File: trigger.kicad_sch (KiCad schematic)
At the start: 0 parts

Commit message: Chose amplifiers
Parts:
- added R23: R, symbol Device:R
- added U2: LTC6754xSC6, Package_TO_SOT_SMD:SOT-363_SC-70-6, symbol Comparator:LTC6754xSC6
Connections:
- new net: R23.1, U2.3 (+)
- new net AN_TRIGGER: U2.4 (-)
- new net AN_TRIGGER_N: U2.6 (~{Q})
- new net AN_TRIGGER_P: U2.1 (Q)
- new net TRIGGER_LEVEL: R23.2

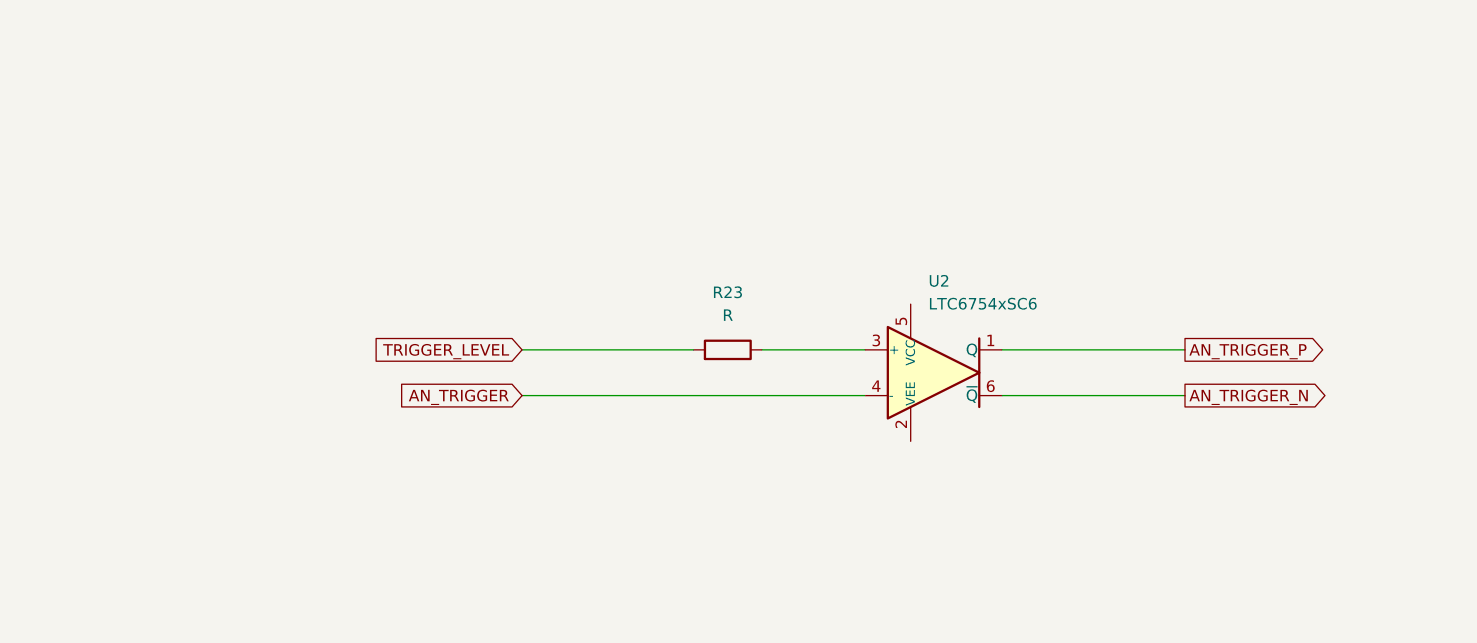
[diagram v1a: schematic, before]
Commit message: Move the trigger
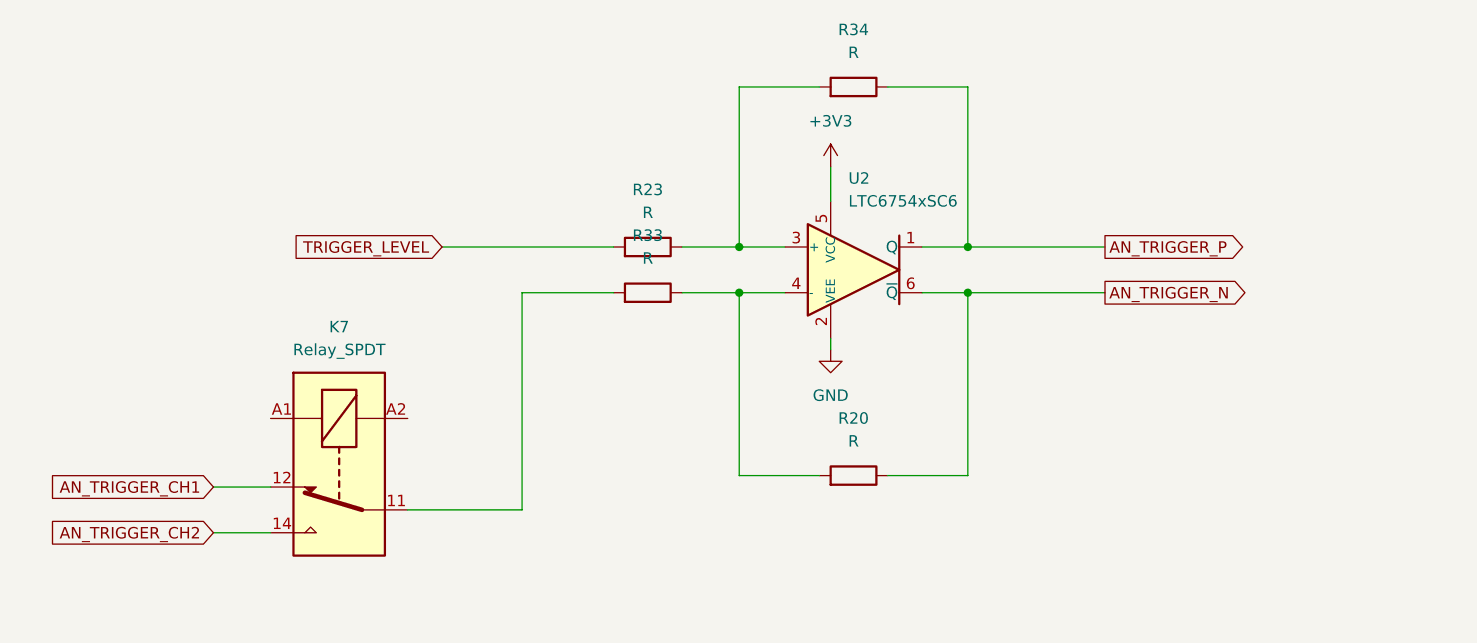
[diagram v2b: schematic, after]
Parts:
- added K7: Relay_SPDT, symbol Relay:Relay_SPDT
- added R20, R33, R34: R, symbol Device:R
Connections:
- net AN_TRIGGER_N: now also R20.1
- net AN_TRIGGER_P: now also R34.1
- net at R23.1, U2.3 (+): now also R34.2
- net GND: now reaches U2.2 (VEE)
- net +3V3: now reaches U2.5 (VCC)
- net AN_TRIGGER: no longer names the net of U2.4 (-)
- net AN_TRIGGER: now also R20.2, R33.1
- new net: K7.11, R33.2
- new net AN_TRIGGER_CH1: K7.12
- new net AN_TRIGGER_CH2: K7.14
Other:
- moved on the sheet: R23, U2

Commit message: Add things to MCU on the board
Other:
- moved on the sheet: K7, R20, R23, R33, R34, U2
